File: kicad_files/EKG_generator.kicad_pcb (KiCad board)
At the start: 2 copper layers, 80 x 104.5 mm, 18 parts, among them J1 WYJŚCIE_EKG, U1 XIAO-ESP32-C6-DIP, U2 DM-OLED096-636, U3 LM358P, U4 MCP4725xxx-xCH

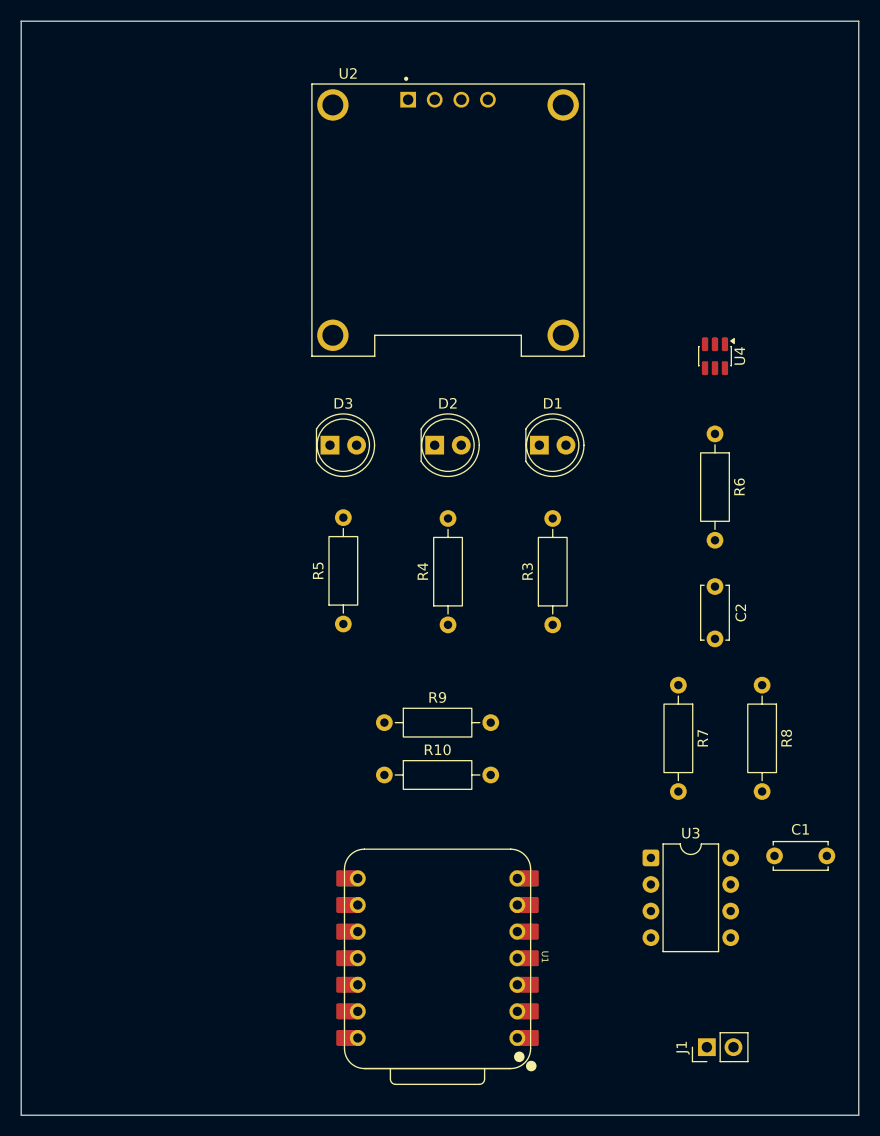
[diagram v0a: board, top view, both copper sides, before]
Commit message: Complete routing on PCB
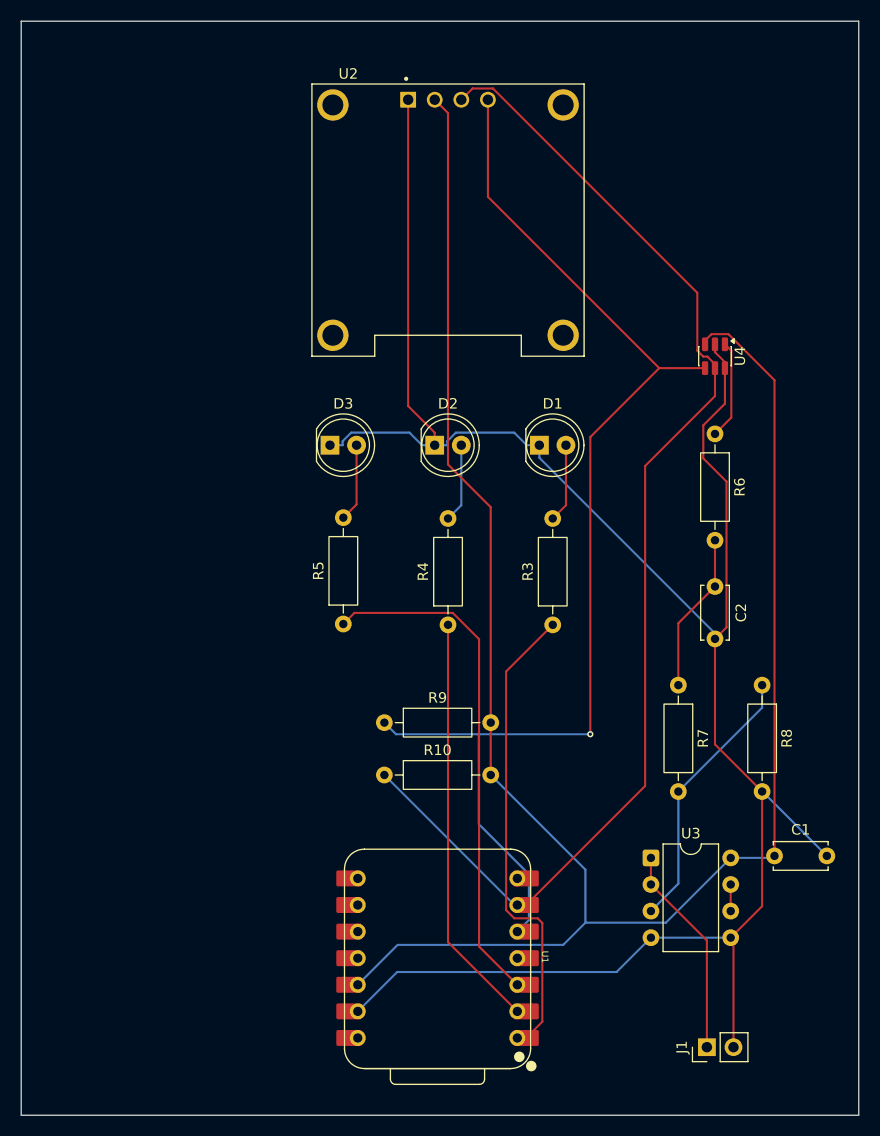
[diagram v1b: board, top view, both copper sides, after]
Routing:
- net GND: track 0.00 -> 203.0 mm
- net +3V3: track 0.00 -> 184.8 mm
- net SDA: track 0.00 -> 116.7 mm, vias 0 -> 1
- net SCL: track 0.00 -> 116.6 mm
- net LED_RED: track 0.00 -> 49.8 mm
- net LED_GREEN: track 0.00 -> 45.5 mm
- net LED_YELLOW: track 0.00 -> 40.5 mm
- net EKG_RAW: track 0.00 -> 26.0 mm
- net EKG_OUT: track 0.00 -> 20.3 mm
- net Net-(C2-Pad1): track 0.00 -> 15.3 mm
- net Net-(U4-VOUT): track 0.00 -> 9.46 mm
- net Net-(D2-A): track 0.00 -> 7.52 mm
- net Net-(D1-A): track 0.00 -> 7.52 mm
- net Net-(D3-A): track 0.00 -> 7.44 mm
- net Net-(U3-Pad6): track 0.00 -> 2.54 mm
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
